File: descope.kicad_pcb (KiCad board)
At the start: 2 copper layers, 17.8 x 12.4 mm, 19 parts, among them Q1 2N3906, Q2 2N3904, Q3 2N3906, Q4 2N3904, Q5 2N3906, Q6 2N3904

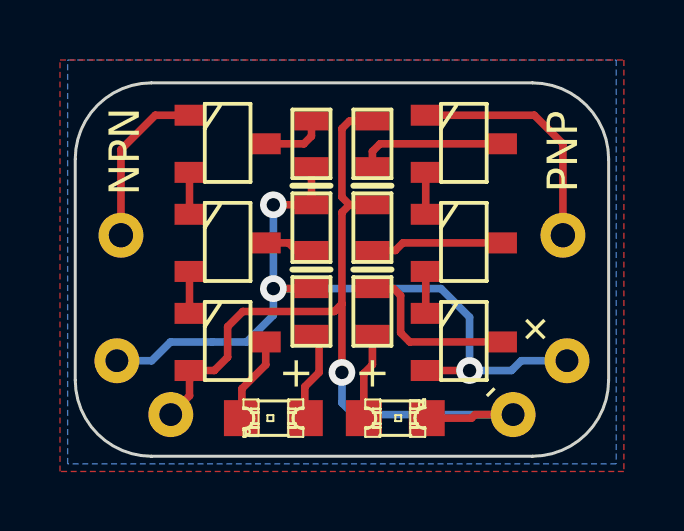
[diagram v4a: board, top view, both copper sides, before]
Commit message: Update for fabrication
* Remove some extraneous traces since we're going back to copper pours.
  Some of the traces are still intact from the non-pour version so that it is
  easy to go back and forth (two traces removed)

* Added a white silk area on the back for notes (like bad/good/sensitivity/config notes)

Fabricator: OSHPark, LLC
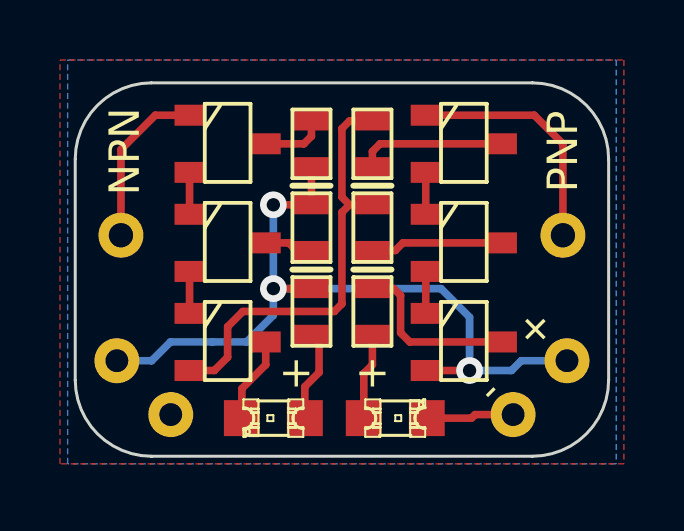
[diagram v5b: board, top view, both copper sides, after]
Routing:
- net GND: track 28.4 -> 17.5 mm, vias 1 -> 0
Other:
- board text added: "Smaller Toy Electroscope open.konspyre.org/selectro R: 2014-10-10 Power: 9V"
- board text removed: "Smaller Toy Electroscope open.konspyre.org/selectro 2014-08-31 V+: 9V"
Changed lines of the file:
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@@
     (thickness 1.6)
     (drawings 17)
-    (tracks 79)
+    (tracks 72)
     (zones 0)
     (modules 19)
@@
     (22 B.Mask user)
     (23 F.Mask user)
-    (24 Dwgs.User user)
-    (25 Cmts.User user)
-    (26 Eco1.User user)
-    (27 Eco2.User user hide)
+    (24 Dwgs.User user hide)
+    (25 Cmts.User user hide)
+    (26 Eco1.User user hide)
+    (27 Eco2.User user)
     (28 Edge.Cuts user)
   )
@@
     (pad_to_mask_clearance 0)
     (aux_axis_origin 0 0)
-    (visible_elements 7FFFFFBF)
+    (visible_elements 7FFFFFBB)
     (pcbplotparams
       (layerselection 284196865)
@@
     (effects (font (size 1.016 1.016) (thickness 0.254)))
   )
-  (gr_text "Smaller Toy Electroscope\nopen.konspyre.org/selectro\n2014-08-31\n\nV+: 9V" (at 154.686 173.101) (layer B.SilkS)
+  (gr_text "Smaller Toy Electroscope\nopen.konspyre.org/selectro\nR: 2014-10-10 Power: 9V" (at 154.686 173.101) (layer B.SilkS)
     (effects (font (size 0.762 0.762) (thickness 0.127)) (justify mirror))
   )
@@
     (effects (font (size 1.016 1.016) (thickness 0.254)))
   )
-  (segment (start 149.606 181.8005) (end 149.606 182.644052) (width 0.254) (layer F.Cu) (net 1))
-  (segment (start 149.606 182.644052) (end 148.980026 183.270026) (width 0.254) (layer F.Cu) (net 1))
   (segment (start 154.432 179.832) (end 154.686 179.578) (width 0.254) (layer F.Cu) (net 1))
   (segment (start 151.384 179.832) (end 154.432 179.832) (width 0.254) (layer F.Cu) (net 1))
   (segment (start 160.391974 183.270026) (end 159.121974 183.270026) (width 0.254) (layer F.Cu) (net 1))
+  (segment (start 159.004 183.388) (end 157.51302 183.388) (width 0.254) (layer F.Cu) (net 1))
   (segment (start 159.121974 183.270026) (end 159.004 183.388) (width 0.254) (layer F.Cu) (net 1))
-  (segment (start 159.004 183.388) (end 157.51302 183.388) (width 0.254) (layer F.Cu) (net 1))
-  (segment (start 154.686 181.864) (end 154.686 182.88) (width 0.254) (layer B.Cu) (net 1))
-  (segment (start 154.686 182.88) (end 155.076026 183.270026) (width 0.254) (layer B.Cu) (net 1))
-  (segment (start 155.076026 183.270026) (end 160.391974 183.270026) (width 0.254) (layer B.Cu) (net 1))
-  (segment (start 154.686 179.578) (end 154.686 181.864) (width 0.254) (layer F.Cu) (net 1))
-  (via (at 154.686 181.864) (size 0.889) (layers F.Cu B.Cu) (net 1))
   (segment (start 155.702 176.276) (end 154.94 176.276) (width 0.254) (layer F.Cu) (net 1))
   (segment (start 154.94 176.276) (end 154.686 176.53) (width 0.254) (layer F.Cu) (net 1))
@@
     (connect_pads (clearance 0.1524))
     (min_thickness 0.1524)
-    (fill (arc_segments 16) (thermal_gap 0.508) (thermal_bridge_width 0.3))
+    (fill (arc_segments 32) (thermal_gap 0.508) (thermal_bridge_width 0.3))
     (polygon
       (pts
@@
     (connect_pads (clearance 0.1524))
     (min_thickness 0.1524)
-    (fill (arc_segments 16) (thermal_gap 0.508) (thermal_bridge_width 0.3))
+    (fill (arc_segments 32) (thermal_gap 0.508) (thermal_bridge_width 0.3))
     (polygon
       (pts
-        (xy 164.084 185.166) (xy 145.288 185.166) (xy 145.288 171.45) (xy 164.084 171.45)
+        (xy 164.084 184.912) (xy 145.288 184.912) (xy 145.288 171.45) (xy 164.084 171.45)
       )
     )
+  )
+  (zone (net 0) (net_name "") (layer B.SilkS) (hatch edge 0.508)
+    (connect_pads (clearance 0.1524))
+    (min_thickness 0.1524)
+    (fill (arc_segments 32) (thermal_gap 0.508) (thermal_bridge_width 0.3))
+    (polygon
+      (pts
+        (xy 159.258 178.562) (xy 150.368 178.562) (xy 150.368 176.784) (xy 159.258 176.784)
+      )
+    )
